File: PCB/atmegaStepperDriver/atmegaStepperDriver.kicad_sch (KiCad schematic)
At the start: 77 parts, among them J1 General power, J2 Motor Output, J3 Motor power, J4 Conn_01x02_Pin, J5 Reset Header, J6 I2C Communication pins, J8 Conn_01x06_Socket, J9 Stepper communication pins, Q1 TIP42C, Q10 BC547, Q11 BC557, Q12 TIP41C, Q13 TIP42C, Q14 BC547, Q15 BC557, Q16 TIP41C, Q2 TIP41C, Q3 TIP42C, Q4 TIP42C, Q5 BC547, Q6 BC547, Q7 BC557, Q8 TIP41C, Q9 BC557, U1 ATmega328P-P, U2 LM7805_TO220, Y1 Crystal

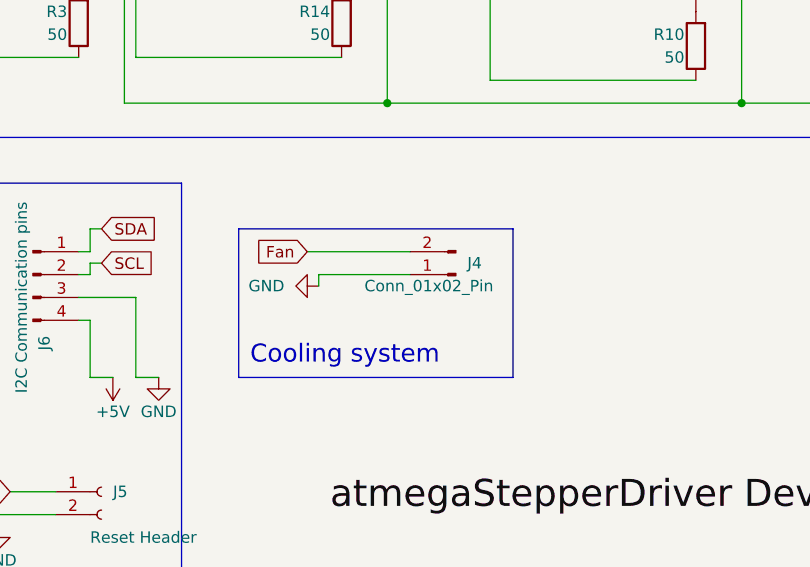
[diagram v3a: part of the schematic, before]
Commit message: added transistor for fan; final checks; Gerber files ready; V0.8.2
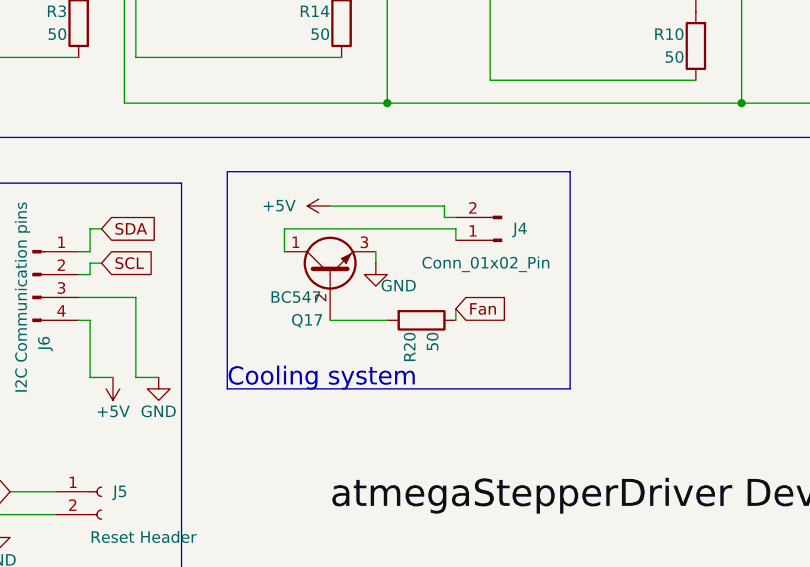
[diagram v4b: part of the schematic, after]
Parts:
- added Q17: BC547, Package_TO_SOT_THT:TO-92_Inline, symbol Transistor_BJT:BC547
- added R20: 50, Resistor_THT:R_Axial_DIN0207_L6.3mm_D2.5mm_P10.16mm_Horizontal, symbol Device:R
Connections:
- net +5V: now also J4.2 (Pin_2)
- net Fan: now also R20.1; no longer J4.2 (Pin_2)
- net GND: now also Q17.3 (E); no longer J4.1 (Pin_1)
- new net: Q17.2 (B), R20.2
- new net: J4.1 (Pin_1), Q17.1 (C)
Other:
- moved on the sheet: J4
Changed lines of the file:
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@@
     (title "atmegaStepperDriver Developer board")
     (date "2023-08-30")
-    (rev "V0.8.1")
+    (rev "V0.8.2")
   )
   (junction (at 187.96 130.81) (diameter 0) (color 0 0 0 0)
@@
     (stroke (width 0) (type default))
   )
+  (wire (pts (xy 176.53 147.32) (xy 176.53 144.78))
+    (stroke (width 0) (type default))
+  )
   (wire (pts (xy 54.61 52.07) (xy 58.42 52.07))
     (stroke (width 0) (type default))
@@
     (stroke (width 0) (type default))
   )
+  (wire (pts (xy 176.53 144.78) (xy 195.58 144.78))
+    (stroke (width 0) (type default))
+  )
   (wire (pts (xy 100.33 180.34) (xy 100.33 167.64))
     (stroke (width 0) (type default))
@@
     (stroke (width 0) (type default))
   )
+  (wire (pts (xy 186.69 147.32) (xy 186.69 148.59))
+    (stroke (width 0) (type default))
+  )
   (wire (pts (xy 160.02 152.4) (xy 153.67 152.4))
     (stroke (width 0) (type default))
@@
     (stroke (width 0) (type default))
   )
-  (wire (pts (xy 180.34 149.86) (xy 190.5 149.86))
-    (stroke (width 0) (type default))
-  )
   (wire (pts (xy 151.13 69.85) (xy 151.13 72.39))
     (stroke (width 0) (type default))
@@
     (stroke (width 0) (type default))
   )
+  (wire (pts (xy 195.58 154.94) (xy 195.58 153.67))
+    (stroke (width 0) (type default))
+  )
   (wire (pts (xy 151.13 69.85) (xy 148.59 69.85))
     (stroke (width 0) (type default))
   )
+  (wire (pts (xy 195.58 144.78) (xy 195.58 146.05))
+    (stroke (width 0) (type default))
+  )
   (wire (pts (xy 144.78 22.86) (xy 144.78 24.13))
     (stroke (width 0) (type default))
@@
     (stroke (width 0) (type default))
   )
+  (wire (pts (xy 194.31 143.51) (xy 194.31 142.24))
+    (stroke (width 0) (type default))
+  )
   (wire (pts (xy 21.59 46.99) (xy 21.59 49.53))
     (stroke (width 0) (type default))
@@
     (stroke (width 0) (type default))
   )
-  (wire (pts (xy 180.34 149.86) (xy 180.34 151.13))
-    (stroke (width 0) (type default))
-  )
   (wire (pts (xy 57.15 107.95) (xy 57.15 110.49))
     (stroke (width 0) (type default))
@@
     (stroke (width 0) (type default))
   )
+  (wire (pts (xy 194.31 142.24) (xy 181.61 142.24))
+    (stroke (width 0) (type default))
+  )
   (wire (pts (xy 100.33 106.68) (xy 100.33 107.95))
     (stroke (width 0) (type default))
@@
     (stroke (width 0) (type default))
   )
-  (wire (pts (xy 179.07 147.32) (xy 190.5 147.32))
+  (wire (pts (xy 194.31 143.51) (xy 195.58 143.51))
+    (stroke (width 0) (type default))
+  )
+  (wire (pts (xy 181.61 154.94) (xy 187.96 154.94))
     (stroke (width 0) (type default))
   )
@@
     (fill (type none))
   )
-  (rectangle (start 171.45 144.78) (end 201.93 161.29)
+  (rectangle (start 170.18 138.43) (end 208.28 162.56)
     (stroke (width 0) (type default))
     (fill (type none))
@@
     (effects (font (size 2 2)) (justify left bottom))
   )
-  (text "Cooling system\n" (at 172.72 160.02 0)
+  (text "Cooling system\n" (at 170.18 162.56 0)
     (effects (font (size 2 2)) (justify left bottom))
   )
@@
     )
   )
-  (global_label "Fan" (shape input) (at 179.07 147.32 180) (fields_autoplaced)
-    (effects (font (size 1.27 1.27)) (justify right))
-    (property "Intersheetrefs" "${INTERSHEET_REFS}" (at 172.6982 147.32 0)
-      (effects (font (size 1.27 1.27)) (justify right) hide)
-    )
-  )
   (global_label "output !B" (shape input) (at 217.17 113.03 180) (fields_autoplaced)
     (effects (font (size 1.27 1.27)) (justify right))
@@
     )
   )
+  (global_label "Fan" (shape input) (at 195.58 153.67 0) (fields_autoplaced)
+    (effects (font (size 1.27 1.27)) (justify left))
+    (property "Intersheetrefs" "${INTERSHEET_REFS}" (at 201.9518 153.67 0)
+      (effects (font (size 1.27 1.27)) (justify left) hide)
+    )
+  )
   (global_label "Rotation" (shape input) (at 66.04 110.49 0) (fields_autoplaced)
     (effects (font (size 1.27 1.27)) (justify left))
@@
     )
   )
+  (symbol (lib_id "Device:R") (at 191.77 154.94 270) (unit 1)
+    (in_bom yes) (on_board yes) (dnp no)
+    (property "Reference" "R20" (at 190.5 156.21 0)
+      (effects (font (size 1.27 1.27)) (justify left))
+    )
+    (property "Value" "50" (at 193.04 156.21 0)
+      (effects (font (size 1.27 1.27)) (justify left))
+    )
+    (property "Footprint" "Resistor_THT:R_Axial_DIN0207_L6.3mm_D2.5mm_P10.16mm_Horizontal" (at 191.77 153.162 90)
+      (effects (font (size 1.27 1.27)) hide)
+    )
+    (property "Datasheet" "~" (at 191.77 154.94 0)
+      (effects (font (size 1.27 1.27)) hide)
+    )
+    (pin "1")
+    (pin "2")
+    (instances
+      (project "atmegaStepperDriver"
+        (path "/c84e7e69-c1fd-4499-93bc-6ad0c4ebade1"
+          (reference "R20") (unit 1)
+        )
+      )
+    )
+  )
   (symbol (lib_id "Transistor_BJT:BC547") (at 143.51 72.39 90) (unit 1)
     (in_bom yes) (on_board yes) (dnp no)
@@
     )
   )
+  (symbol (lib_id "power:+5V") (at 181.61 142.24 90) (unit 1)
+    (in_bom yes) (on_board yes) (dnp no) (fields_autoplaced)
+    (property "Reference" "#PWR028" (at 185.42 142.24 0)
+      (effects (font (size 1.27 1.27)) hide)
+    )
+    (property "Value" "+5V" (at 177.8 142.24 90)
+      (effects (font (size 1.27 1.27)) (justify left))
+    )
+    (property "Footprint" "" (at 181.61 142.24 0)
+      (effects (font (size 1.27 1.27)) hide)
+    )
+    (property "Datasheet" "" (at 181.61 142.24 0)
+      (effects (font (size 1.27 1.27)) hide)
+    )
+    (pin "1")
+    (instances
+      (project "atmegaStepperDriver"
+        (path "/c84e7e69-c1fd-4499-93bc-6ad0c4ebade1"
+          (reference "#PWR028") (unit 1)
+        )
+      )
+    )
+  )
   (symbol (lib_id "Connector:Conn_01x04_Pin") (at 148.59 149.86 0) (unit 1)
     (in_bom yes) (on_board yes) (dnp no)
@@
     )
   )
+  (symbol (lib_id "Transistor_BJT:BC547") (at 181.61 149.86 90) (unit 1)
+    (in_bom yes) (on_board yes) (dnp no)
+    (property "Reference" "Q17" (at 179.07 154.94 90)
+      (effects (font (size 1.27 1.27)))
+    )
+    (property "Value" "BC547" (at 177.8 152.4 90)
+      (effects (font (size 1.27 1.27)))
+    )
+    (property "Footprint" "Package_TO_SOT_THT:TO-92_Inline" (at 183.515 144.78 0)
+      (effects (font (size 1.27 1.27) italic) (justify left) hide)
+    )
+    (property "Datasheet" "https://www.onsemi.com/pub/Collateral/BC550-D.pdf" (at 181.61 149.86 0)
+      (effects (font (size 1.27 1.27)) (justify left) hide)
+    )
+    (pin "1")
+    (pin "2")
+    (pin "3")
+    (instances
+      (project "atmegaStepperDriver"
+        (path "/c84e7e69-c1fd-4499-93bc-6ad0c4ebade1"
+          (reference "Q17") (unit 1)
+        )
+      )
+    )
+  )
   (symbol (lib_id "Transistor_BJT:TIP42C") (at 203.2 66.04 90) (unit 1)
     (in_bom yes) (on_board yes) (dnp no)
@@
     )
   )
-  (symbol (lib_id "power:GND") (at 180.34 151.13 270) (unit 1)
-    (in_bom yes) (on_board yes) (dnp no) (fields_autoplaced)
-    (property "Reference" "#PWR029" (at 173.99 151.13 0)
+  (symbol (lib_id "power:GND") (at 186.69 148.59 0) (unit 1)
+    (in_bom yes) (on_board yes) (dnp no)
+    (property "Reference" "#PWR029" (at 186.69 154.94 0)
       (effects (font (size 1.27 1.27)) hide)
     )
-    (property "Value" "GND" (at 176.53 151.13 90)
-      (effects (font (size 1.27 1.27)) (justify right))
+    (property "Value" "GND" (at 189.23 151.13 0)
+      (effects (font (size 1.27 1.27)))
     )
-    (property "Footprint" "" (at 180.34 151.13 0)
+    (property "Footprint" "" (at 186.69 148.59 0)
       (effects (font (size 1.27 1.27)) hide)
     )
-    (property "Datasheet" "" (at 180.34 151.13 0)
+    (property "Datasheet" "" (at 186.69 148.59 0)
       (effects (font (size 1.27 1.27)) hide)
     )
@@
     )
   )
-  (symbol (lib_id "Connector:Conn_01x02_Pin") (at 195.58 149.86 180) (unit 1)
+  (symbol (lib_id "Connector:Conn_01x02_Pin") (at 200.66 146.05 180) (unit 1)
     (in_bom yes) (on_board yes) (dnp no)
-    (property "Reference" "J4" (at 196.85 148.59 0)
+    (property "Reference" "J4" (at 201.93 144.78 0)
       (effects (font (size 1.27 1.27)) (justify right))
     )
-    (property "Value" "Conn_01x02_Pin" (at 185.42 151.13 0)
+    (property "Value" "Conn_01x02_Pin" (at 191.77 148.59 0)
       (effects (font (size 1.27 1.27)) (justify right))
     )
-    (property "Footprint" "Connector_PinHeader_2.54mm:PinHeader_1x02_P2.54mm_Vertical" (at 195.58 149.86 0)
+    (property "Footprint" "Connector_PinHeader_2.54mm:PinHeader_1x02_P2.54mm_Vertical" (at 200.66 146.05 0)
       (effects (font (size 1.27 1.27)) hide)
     )
-    (property "Datasheet" "~" (at 195.58 149.86 0)
+    (property "Datasheet" "~" (at 200.66 146.05 0)
       (effects (font (size 1.27 1.27)) hide)
     )

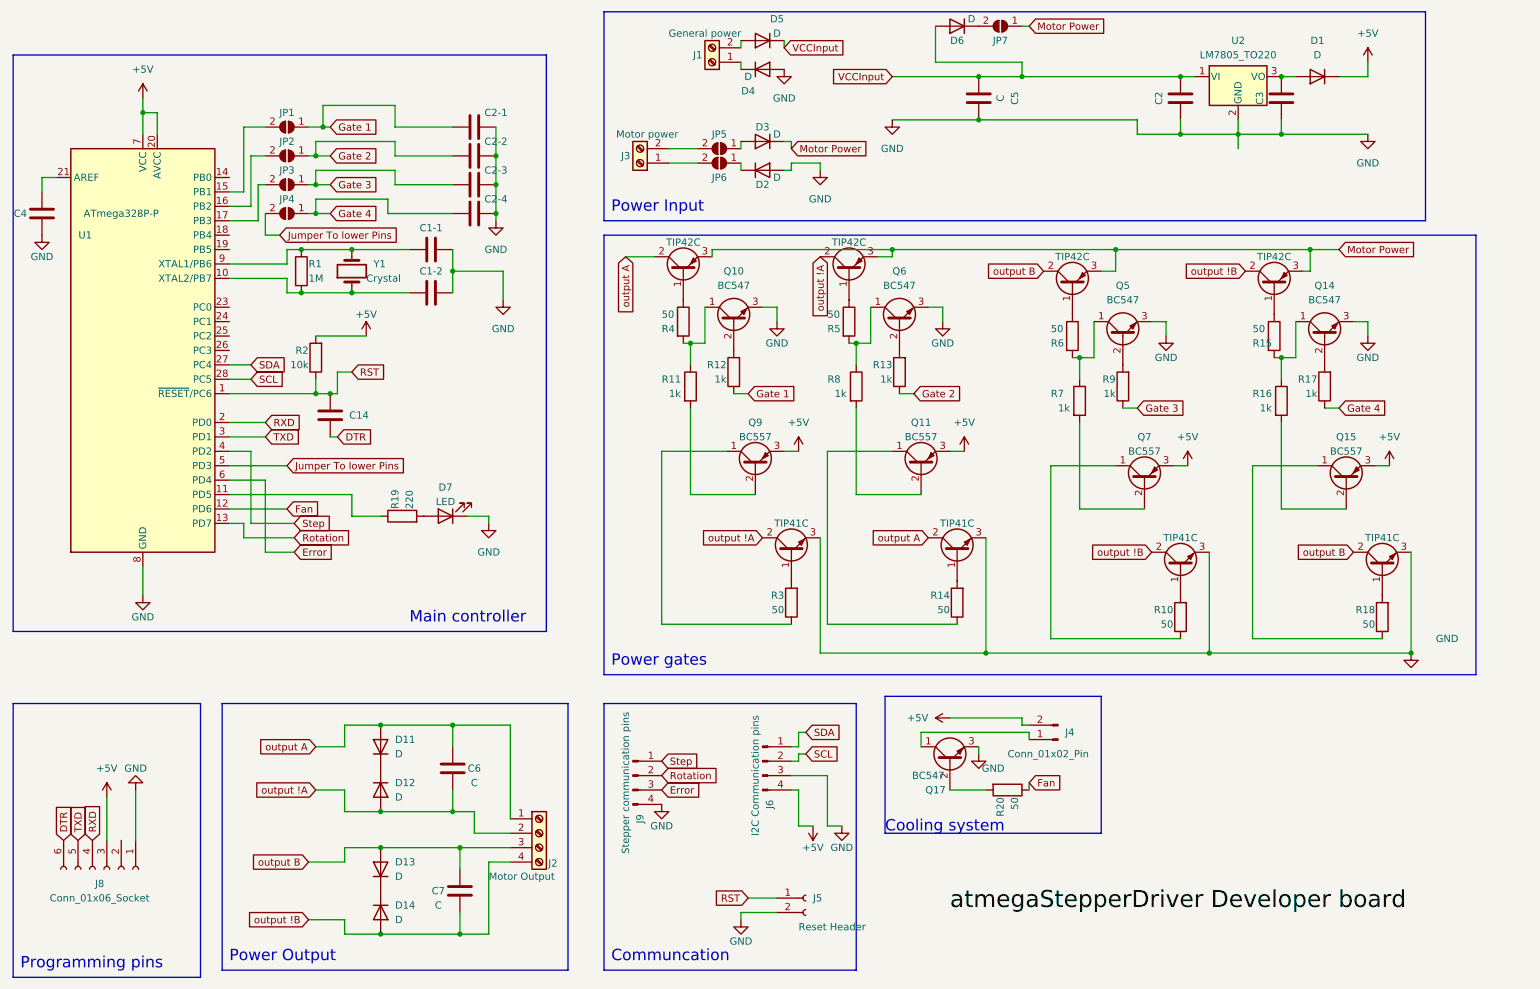
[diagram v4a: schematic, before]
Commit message: fixed bad transistors; readme; V0.8.3
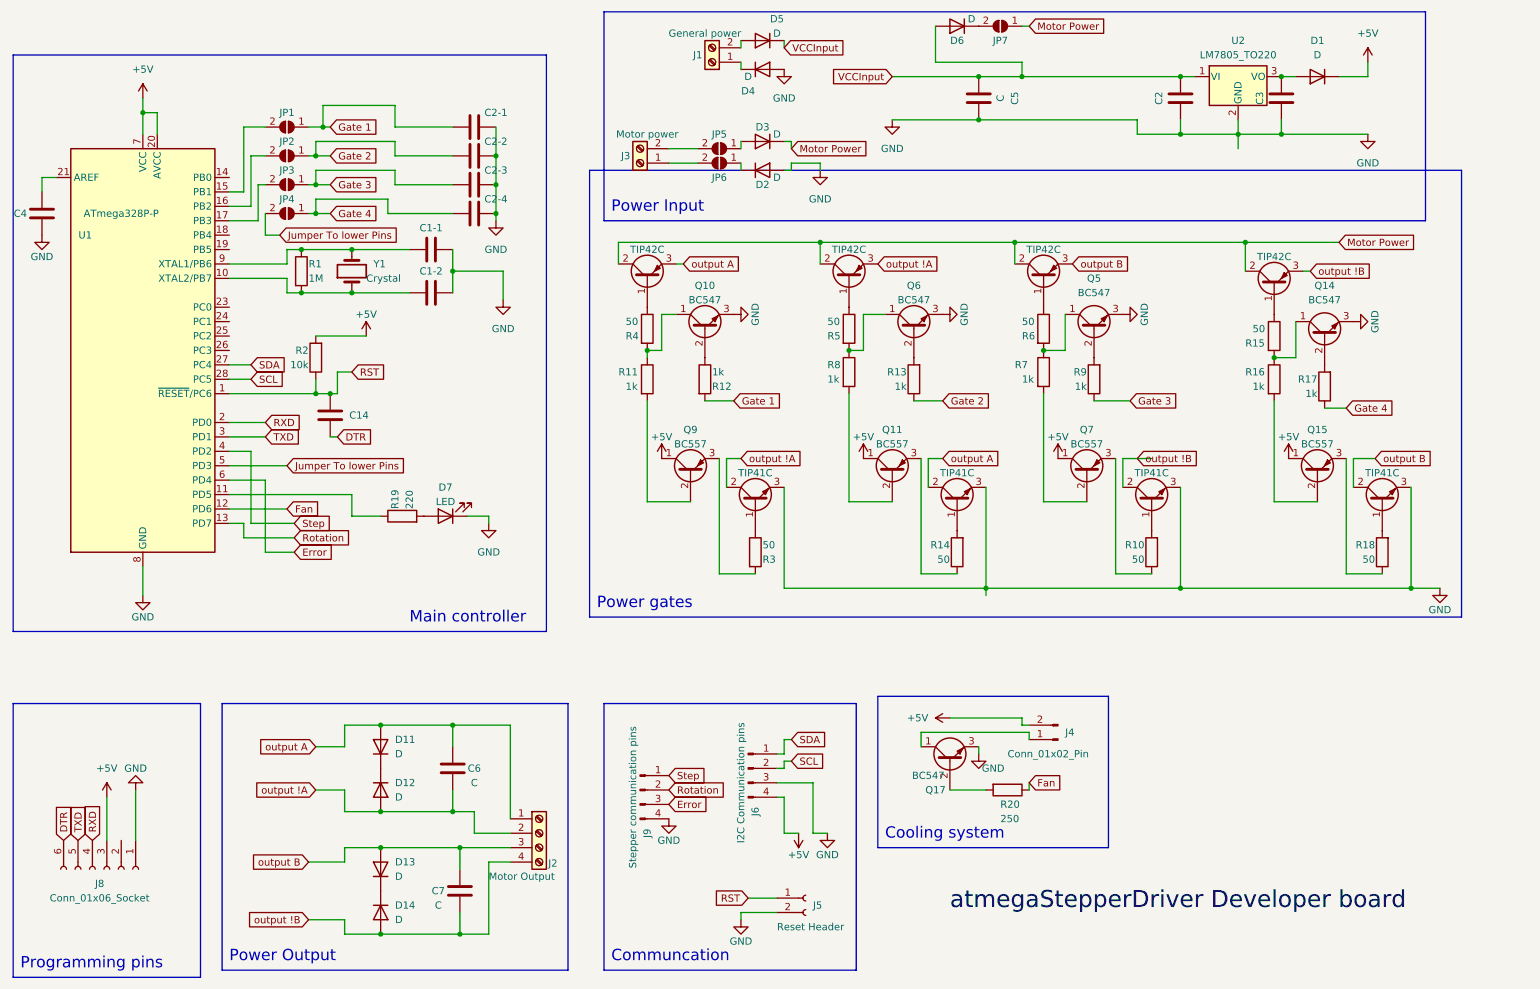
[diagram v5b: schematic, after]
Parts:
- Q10, Q11, Q14, Q15, Q5, Q6, Q7, Q9: footprint Package_TO_SOT_THT:TO-92_Inline -> Package_TO_SOT_THT:TO-92_Inline_Wide
- R20: value 50 -> 250
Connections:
- net +5V: now also Q11.1 (C), Q15.1 (C), Q7.1 (C), Q9.1 (C); no longer Q11.3 (E), Q15.3 (E), Q7.3 (E), Q9.3 (E)
- net Gate 1: now also R12.2; no longer R12.1
- net Motor Power: now also Q1.2 (C), Q13.2 (C), Q3.2 (C), Q4.2 (C); no longer Q1.3 (E), Q13.3 (E), Q3.3 (E), Q4.3 (E)
- net output !A: now also Q3.3 (E); no longer Q3.2 (C)
- net output !B: now also Q13.3 (E); no longer Q13.2 (C)
- net output A: now also Q1.3 (E); no longer Q1.2 (C)
- net output B: now also Q4.3 (E); no longer Q4.2 (C)
- net at Q10.2 (B): now also R12.1; no longer R12.2
- net at R14.1: now also Q11.3 (E); no longer Q11.1 (C)
- net at R10.1: now also Q7.3 (E); no longer Q7.1 (C)
- net at Q2.1 (B): now also R3.1; no longer R3.2
- net at R18.1: now also Q15.3 (E); no longer Q15.1 (C)
- new net: Q9.3 (E), R3.2
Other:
- moved on the sheet: J6, J9, Q10, Q11, Q15, Q5, Q6, Q7, Q9, R10, R11, R12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
